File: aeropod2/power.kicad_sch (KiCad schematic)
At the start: 24 parts, among them J1 USB_C_Receptacle_USB2.0_14P, U1 TP4056-42-ESOP8, U2 AMS1117-3.3, U7 MT3608

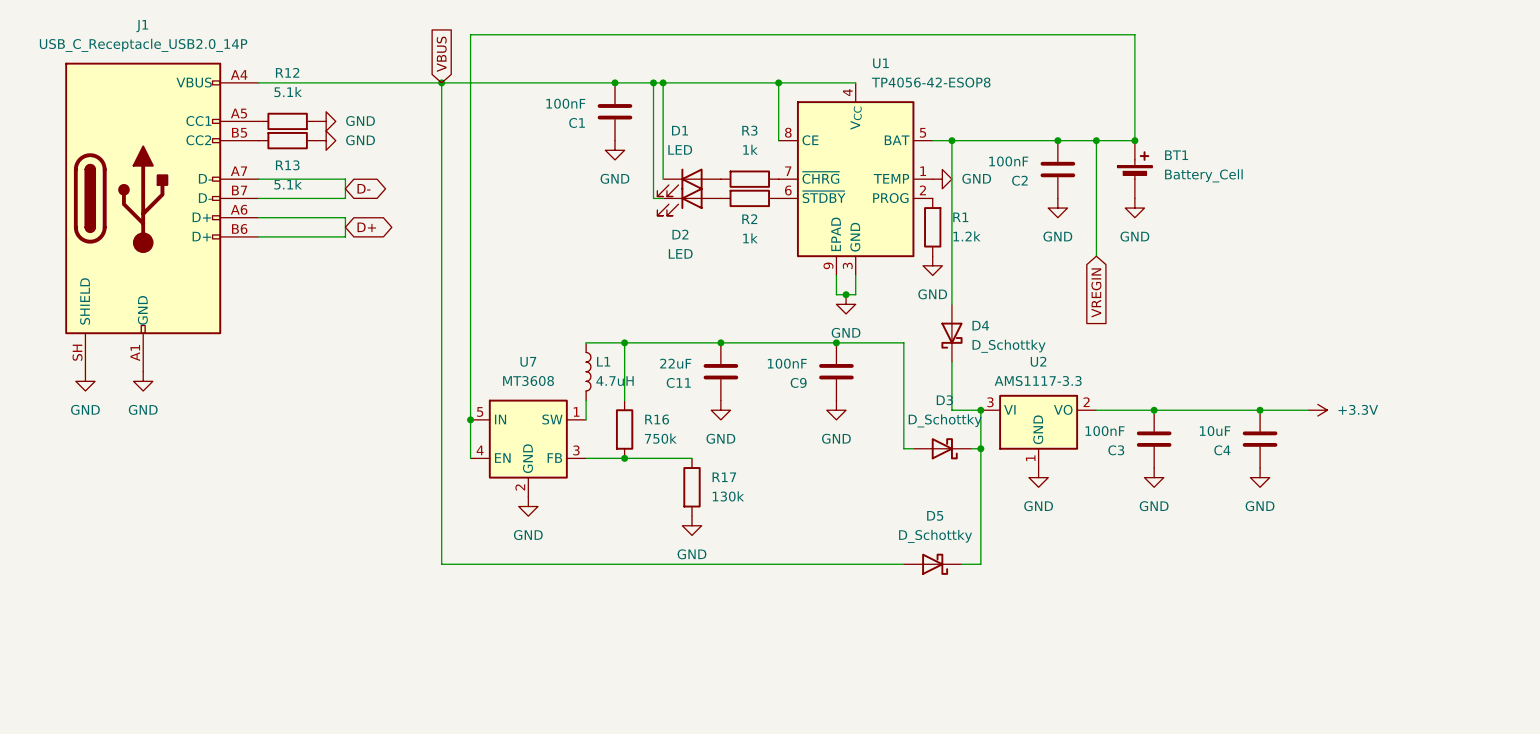
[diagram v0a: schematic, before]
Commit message: Fix schematic faults found in electrical review, add reset/boot buttons
Four faults would have stopped the main board working:

- EN had no pull-up. R4/C5 sat on the unused throw of SW1 while EN was
  left holding only an AC coupled cap, so the module would not have
  booted. R4/C5 now sit on EN, and SW1/SW2 are momentary buttons to
  ground instead of slide switches.
- The microSD was miswired: connections shifted by one pin and CMD tied
  to GND, so no card could ever initialise. The display data line also
  shared a net with the card's DAT0 output. CS now lands on DAT3/CD,
  CMD on IO23 alongside the display, and IO19 is MISO from the card
  alone.
- The boost inductor was never connected to the input rail, so the
  MT3608 had nothing to pump. Rebuilt as VREGIN to L1 to SW plus diode
  anode, with the output caps and feedback divider past the diode.
- The 3.3 V rail had no headroom. R17 is now 100k, putting the boost
  near 5.1 V so the AMS1117 can actually regulate.

Also: backlight control on a new J6 pin 8 driven from IO33, 10k pull-ups
on all five button lines so GPIO35 stops floating, a 100k/100k battery
divider into IO34, both charge LEDs flipped the right way round, 33 ohm
audio series resistors instead of 470, and TP4056 set to about 400 mA.

The CP2102N auto-reset caps are gone. That package brings out RTS but no
DTR, and C30 drove IO0 from CTS, which is an input, so it could not have
worked. Flashing uses the buttons.

Firmware config.h is rewritten against the corrected schematic, and
i2s_output_init now releases the PCM5102A hardware mute on GPIO12, which
nothing was driving.

Schematic passes ERC with no new violations. The PCB has not been
re-laid-out yet, so the main board gerbers are stale; see
ELECTRICAL_REVIEW.md.
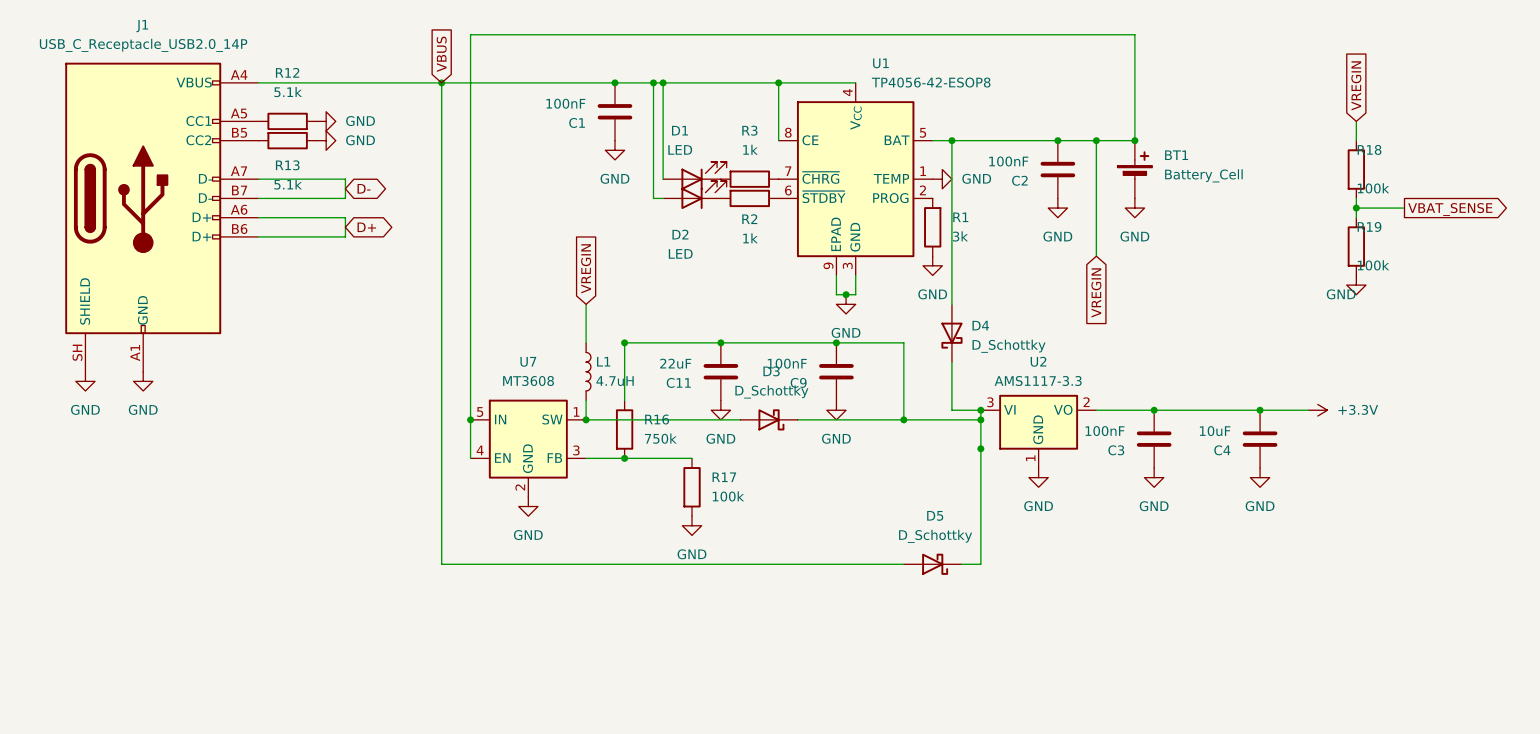
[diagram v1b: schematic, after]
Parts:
- added R18, R19: 100k, Resistor_SMD:R_0402_1005Metric, symbol Device:R
- R1: value 1.2k -> 3k
- R17: value 130k -> 100k
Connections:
- net GND: now also R19.2
- net VBUS: now also D1.2 (A), D2.2 (A); no longer D1.1 (K), D2.1 (K)
- net VREGIN: now also L1.1, R18.1
- net at D3.1 (K), D4.1 (K), D5.1 (K)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: now also C11.2, C9.2, R16.1
- net at R3.2: now also D1.1 (K); no longer D1.2 (A)
- net at L1.2, U7.1 (SW): now also D3.2 (A)
- net at R2.2: now also D2.1 (K); no longer D2.2 (A)
- new net VBAT_SENSE: R18.2, R19.1
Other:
- moved on the sheet: D1, D2, D3

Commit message: Drop button pull-ups and backlight pin, clear ERC, vendor CP2102N footprint
The five button pull-ups are gone. The only line that actually needed one
was B5, because it sat on GPIO35 and GPIO34-39 are input only with no
internal pull-up. B5 now sits on GPIO33, a full GPIO, so the ESP32's own
pull-ups hold all five buttons high and R20-R24 are removed. GPIO35 is
spare.

The display connector goes back to seven pins. There is no backlight
control line, so the module's BL input is tied to 3.3 V and runs at full
brightness. The LEDC setup is removed and display_backlight() is a no-op
so callers do not change.

The five power_pin_not_driven errors are now properly resolved with
PWR_FLAGs on GND, VBUS, VSYS, AVDD and GNDA. To be clear about the VSS
one: that check looks for a power output pin on each rail and finds none
on a rail fed through a diode, ferrite or net tie. It was never a wiring
fault. Before the fixes it named J5 pin 3 CMD, because CMD was wrongly on
the GND net; afterwards it named J5 pin 6 VSS, which is the card's ground
pin and belongs there. The name moved because CMD left the ground net,
which is what the fix was for. Schematic is now 0 errors, 0 warnings.

The microSD wiring was re-verified pin by pin against the SD spec in SPI
mode: DAT2 and DAT1 unused, CS on DAT3/CD, MOSI on CMD, MISO on DAT0,
CLK on pin 5, VDD on pin 4, VSS on GND. All eight correct.

Footprints for every one of the 67 components were checked against what
is on disk. U6 was pointing at a vendor library in a Downloads folder
via a global nickname, so it built here and nowhere else. That library is
now vendored at aeropod2/footprints.pretty with a project fp-lib-table.

Also gitignores KiCad .lck session files.
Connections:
- net VSYS: now reaches C11.2, C9.2, D3.1 (K), D4.1 (K), D5.1 (K), R16.1, U2.3 (VI)

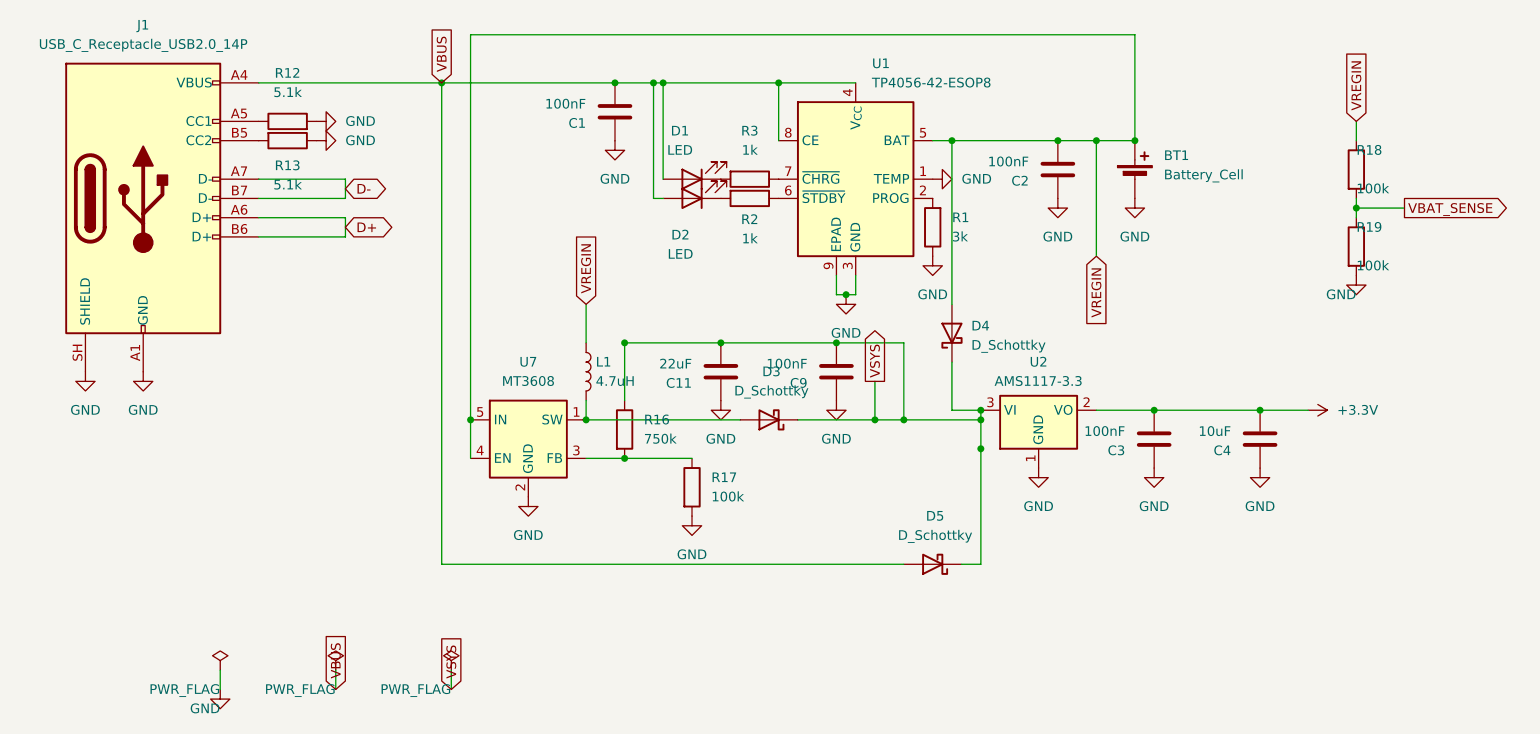
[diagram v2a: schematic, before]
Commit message: Revert schematic, PCB and firmware to the hand-drawn version
Restores aeropod2/*.kicad_sch, aeropod2.kicad_pcb, the firmware pin map
and the BOM to their state at d6429d0, which is byte identical to the
last human-edited revision (2867710). The corrected schematic is still
in history at b35a9fa if any of it is wanted later.

The board file had picked up R18/R19 and the tactile switch footprints
from a schematic update. Nothing hand-made was lost reverting it: track
and via counts were unchanged at 894/147 and the two new parts were
sitting at KiCad's default drop position.

ELECTRICAL_REVIEW.md is rewritten to describe the faults as they stand
in this schematic, and to give the smallest set of layout changes that
makes the board work rather than the full correction.
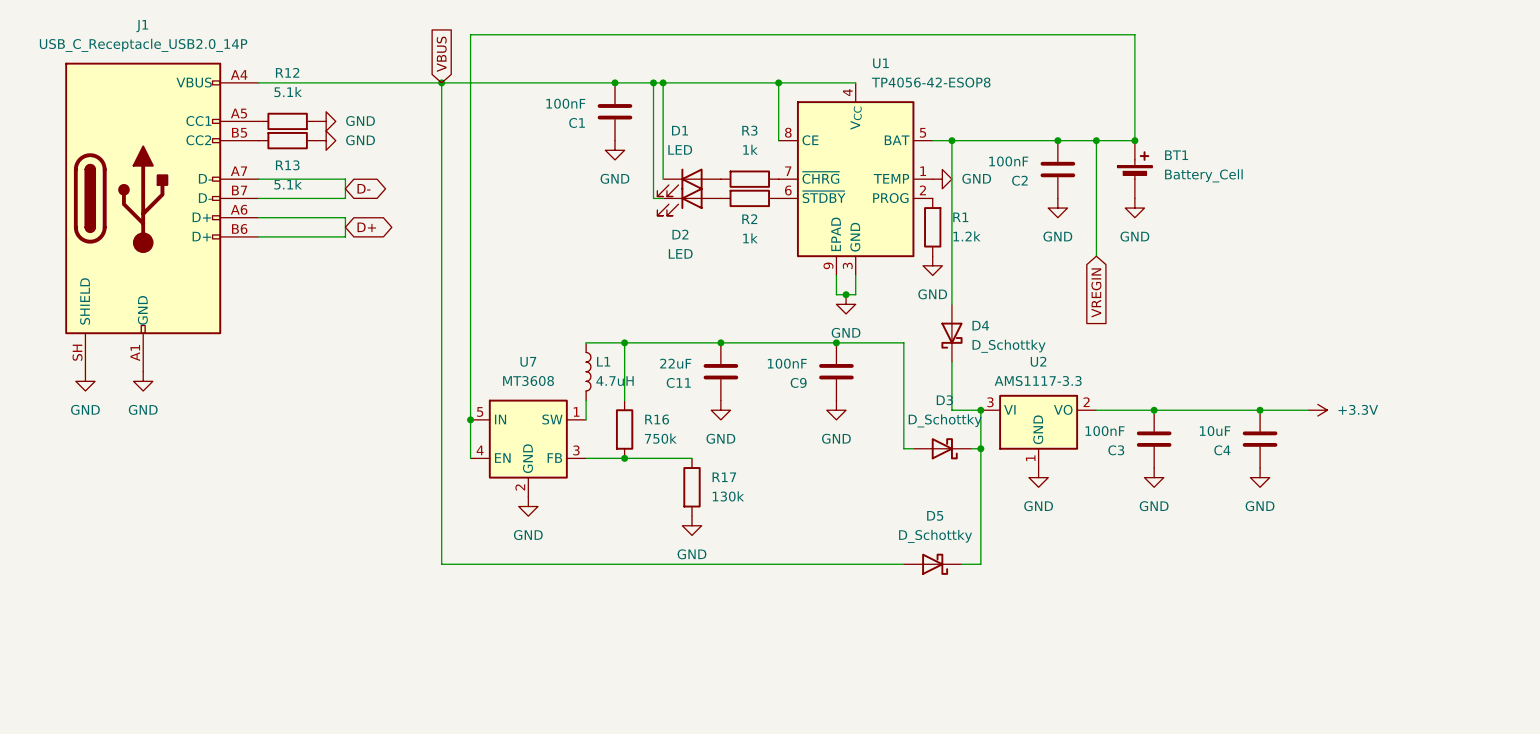
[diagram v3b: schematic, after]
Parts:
- removed R18, R19: 100k, Resistor_SMD:R_0402_1005Metric, symbol Device:R
- R1: value 3k -> 1.2k
- R17: value 100k -> 130k
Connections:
- net VBUS: now also D1.1 (K), D2.1 (K); no longer D1.2 (A), D2.2 (A)
- net VREGIN: no longer L1.1
- net at L1.2, U7.1 (SW): no longer D3.2 (A)
- net at R3.2: now also D1.2 (A); no longer D1.1 (K)
- net at R2.2: now also D2.2 (A); no longer D2.1 (K)
- net VSYS: no longer names the net of D3.1 (K), D4.1 (K), D5.1 (K), U2.3 (VI)
- net VSYS: no longer C11.2, C9.2, R16.1
- new net: C11.2, C9.2, D3.2 (A), L1.1, R16.1
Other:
- moved on the sheet: D1, D2, D3
